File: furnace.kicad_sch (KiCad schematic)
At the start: 32 parts, among them J1 TSW-123-07-T-D, J10 ST7, J2 TSW-123-07-T-D, J3 ST0, J4 ST1, J5 ST2, J6 ST3, J7 ST4, J8 ST5, J9 ST6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

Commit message: furnace.kicad_sch - update schematic description
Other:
- company: (none) -> One Unified Net Limited
- title: Furnace Temperature -> BB Cape: 7 x Voltage Divider ANI
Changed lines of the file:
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@@
 	(paper "A4")
 	(title_block
-		(title "Furnace Temperature")
+		(title "BB Cape: 7 x Voltage Divider ANI")
 		(date "2025-12-26")
 		(rev "1.0")
+		(company "One Unified Net Limited")
+		(comment 1 "Author: Raymond Burkholder")
 	)
 	(junction

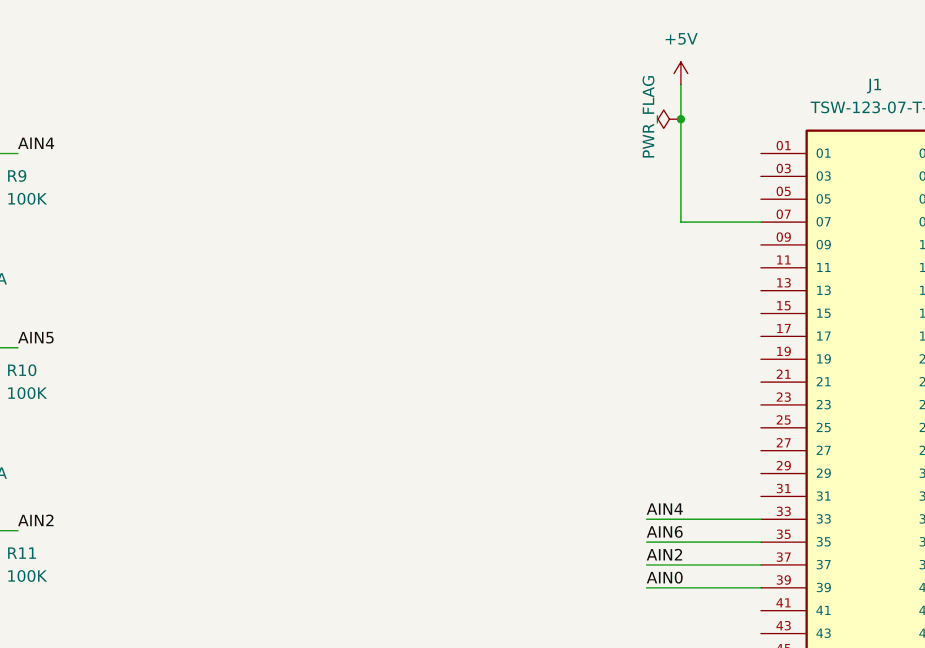
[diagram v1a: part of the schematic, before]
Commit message: furnace.kicad_sch - add sensor references
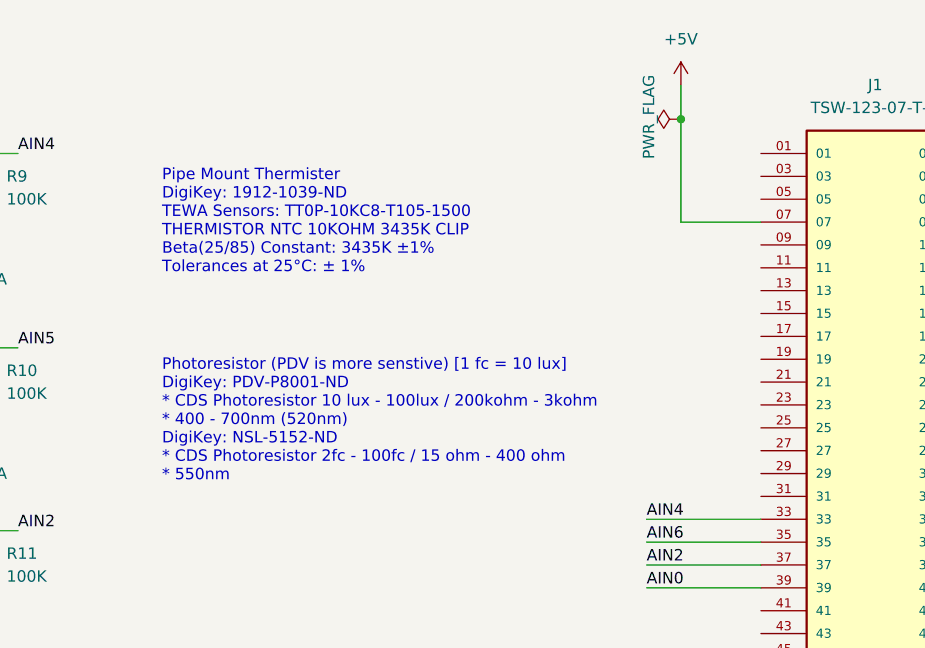
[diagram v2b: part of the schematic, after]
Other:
- note added: "Photoresistor (PDV is more senstive) [1 fc = 10 lux] DigiKey: PDV-P8001-ND * CDS Photoresistor 10 lux - 100lux / 200kohm - 3kohm * 400 - 700nm (520nm) DigiKey: NSL-5152-ND * CDS Photoresistor 2fc - 100fc / 15 ohm - 400 ohm * 550nm"
- note added: "Pipe Mount Thermister DigiKey: 1912-1039-ND TEWA Sensors: TT0P-10KC8-T105-1500 THERMISTOR NTC 10KOHM 3435K CLIP Beta(25/85) Constant: 3435K ±1% Tolerances at 25°C: ± 1%"
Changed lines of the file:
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@@
 		(comment 1 "Author: Raymond Burkholder")
+	)
+	(text "Photoresistor (PDV is more senstive) [1 fc = 10 lux]\nDigiKey: PDV-P8001-ND\n* CDS Photoresistor 10 lux - 100lux / 200kohm - 3kohm\n* 400 - 700nm (520nm)\nDigiKey: NSL-5152-ND\n* CDS Photoresistor 2fc - 100fc / 15 ohm - 400 ohm\n* 550nm\n"
+		(exclude_from_sim no)
+		(at 137.922 60.198 0)
+		(effects
+			(font
+				(size 1.27 1.27)
+			)
+			(justify left)
+		)
+	)
+	(text "Pipe Mount Thermister\nDigiKey: 1912-1039-ND\nTEWA Sensors: TT0P-10KC8-T105-1500\nTHERMISTOR NTC 10KOHM 3435K CLIP\nBeta(25/85) Constant: 3435K ±1%\nTolerances at 25°C: ± 1%"
+		(exclude_from_sim no)
+		(at 137.922 38.1 0)
+		(effects
+			(font
+				(size 1.27 1.27)
+			)
+			(justify left)
+		)
 	)
 	(junction

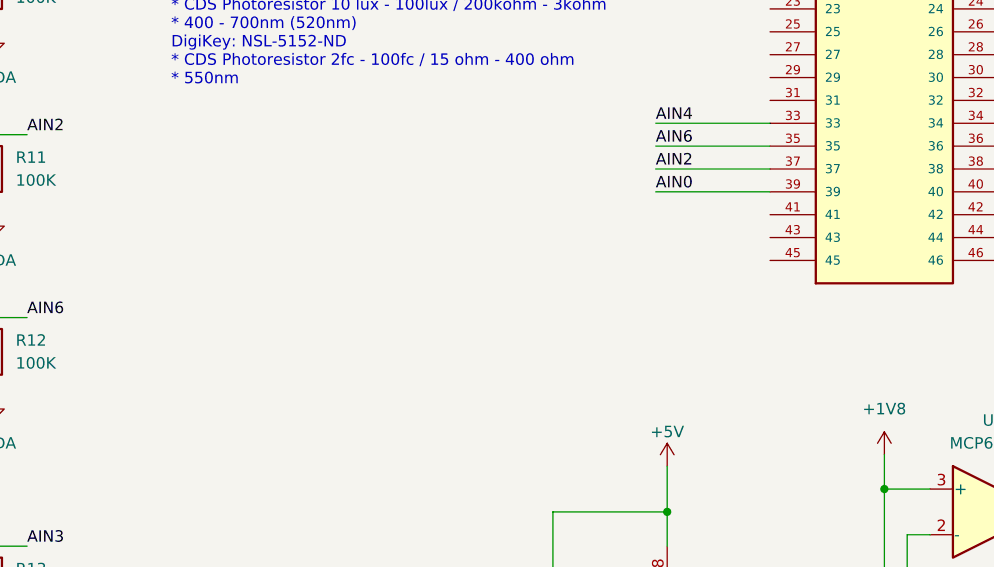
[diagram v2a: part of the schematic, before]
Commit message: furnace.kicad_sch - terminal block and header strip info
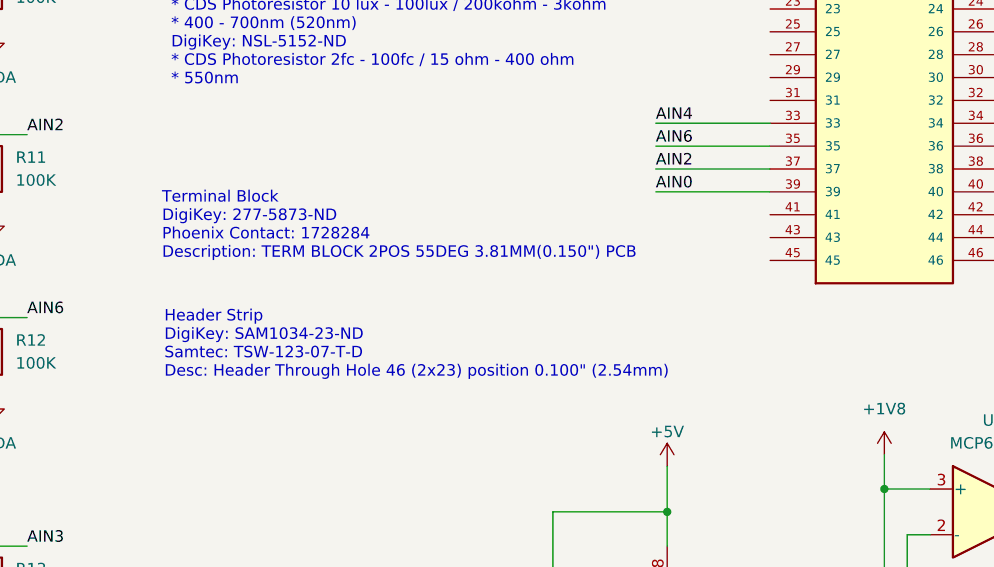
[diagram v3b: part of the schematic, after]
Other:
- note added: "Header Strip DigiKey: SAM1034-23-ND Samtec: TSW-123-07-T-D Desc: Header Through Hole 46 (2x23) position 0.100" (2.54mm)"
- note added: "Terminal Block DigiKey: 277-5873-ND Phoenix Contact: 1728284 Description: TERM BLOCK 2POS 55DEG 3.81MM(0.150") PCB"
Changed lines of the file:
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@@
 		(comment 1 "Author: Raymond Burkholder")
+	)
+	(text "Header Strip\nDigiKey: SAM1034-23-ND\nSamtec: TSW-123-07-T-D\nDesc: Header Through Hole 46 (2x23) position 0.100\" (2.54mm)"
+		(exclude_from_sim no)
+		(at 137.16 95.758 0)
+		(effects
+			(font
+				(size 1.27 1.27)
+			)
+			(justify left)
+		)
 	)
 	(text "Photoresistor (PDV is more senstive) [1 fc = 10 lux]\nDigiKey: PDV-P8001-ND\n* CDS Photoresistor 10 lux - 100lux / 200kohm - 3kohm\n* 400 - 700nm (520nm)\nDigiKey: NSL-5152-ND\n* CDS Photoresistor 2fc - 100fc / 15 ohm - 400 ohm\n* 550nm\n"
@@
 		(effects
 			(font
+				(size 1.27 1.27)
+			)
+			(justify left)
+		)
+	)
+	(text "Terminal Block\nDigiKey: 277-5873-ND\nPhoenix Contact: 1728284\nDescription: TERM BLOCK 2POS 55DEG 3.81MM(0.150\") PCB\n"
+		(exclude_from_sim no)
+		(at 136.906 82.55 0)
+		(effects
+			(font
